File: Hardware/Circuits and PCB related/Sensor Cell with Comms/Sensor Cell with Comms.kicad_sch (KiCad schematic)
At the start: 57 parts, among them J1 Conn_01x02_Shielded, U1 TCAN337, U10 FM24V05, U2 MCP2518FD-xQBB, U3 STM32F103C6Tx, U4 TPS22950x, U5 TPS2421, U6 TPS2421, U7 TMP75B, U8 TMP75B, U9 TMP75B, Y1 DSC6111B

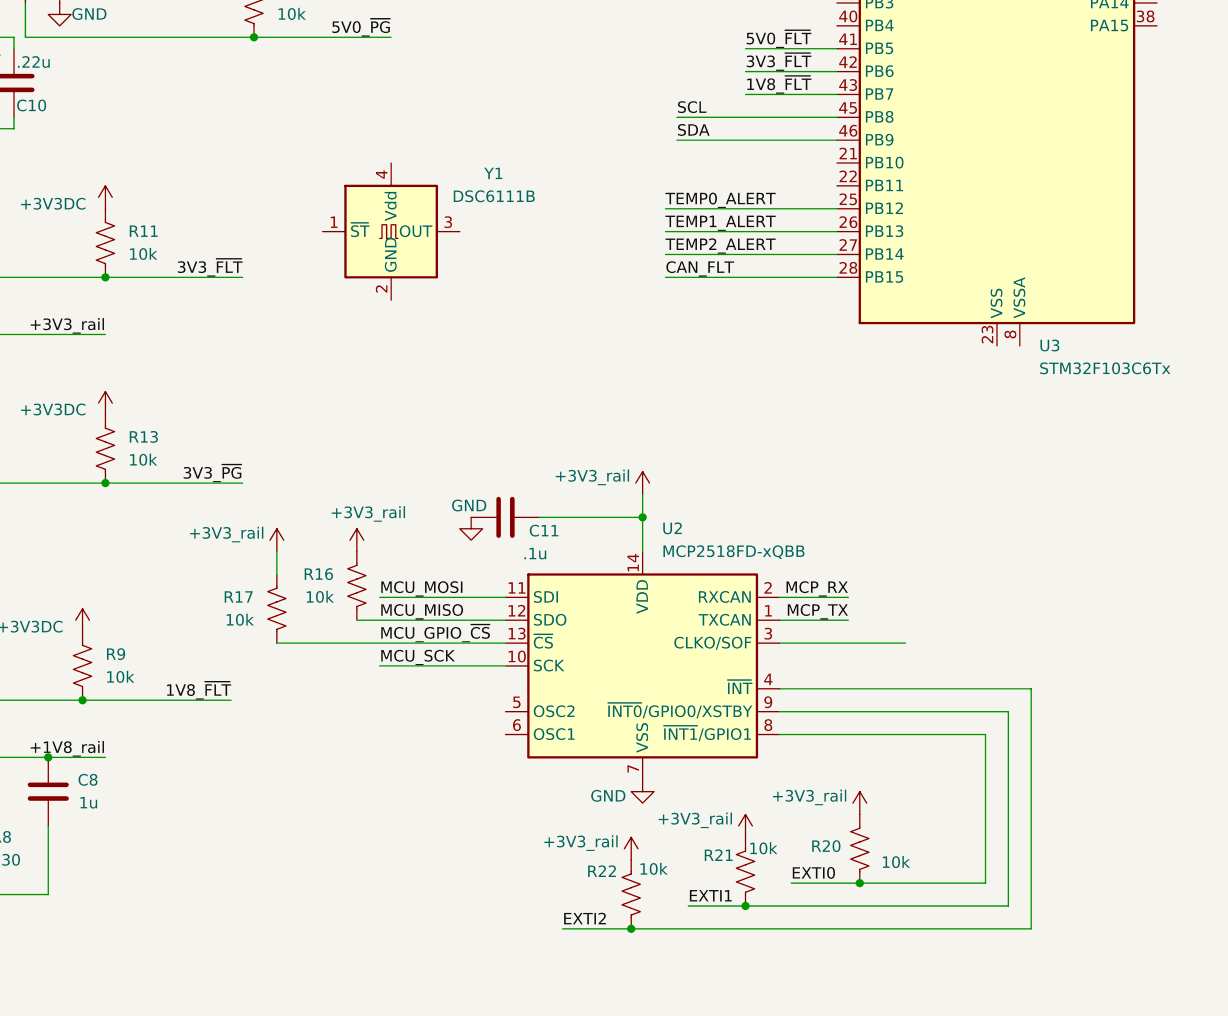
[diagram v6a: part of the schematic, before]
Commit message: Footprint for Osc done, osc wired to MCP and STM wired to Osc. I need to make the pcb now, and then determine what type of connector to use. Things to keep in mind when choosing; Needs to either support power and data, or we can separate out the data and power bus to different connectors. Look into after the interface doc is finalized or closer to completion. Start integration to connect the two small subsystems together for demo
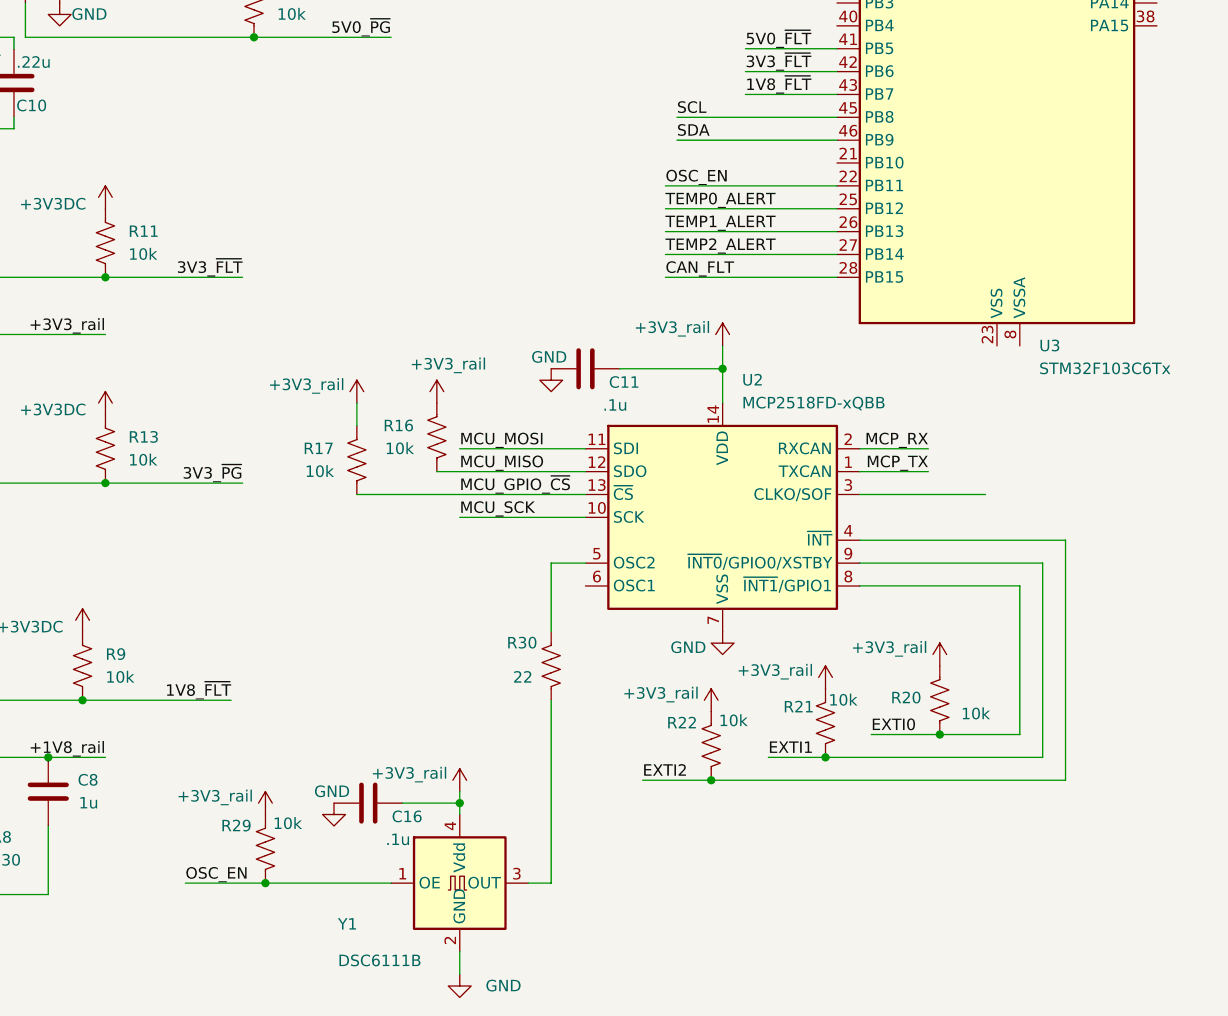
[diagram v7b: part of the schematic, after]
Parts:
- added C16: .1u, Capacitor_SMD:C_0603_1608Metric_Pad1.08x0.95mm_HandSolder, symbol Device:C
- added R29: 10k, Resistor_SMD:R_0603_1608Metric_Pad0.98x0.95mm_HandSolder, symbol Device:R_US
- added R30: 22, Resistor_SMD:R_0603_1608Metric_Pad0.98x0.95mm_HandSolder, symbol Device:R_US
- Y1: footprint footprintLib:VDFN-4_5x3.2mm_P2.54BSC -> Oscillator:Oscillator_SMD_SiT_PQFN-4Pin_2.0x1.6mm
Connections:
- net +3V3_rail: now also Y1.4 (Vdd), C16.2, R29.2
- net GND: now also Y1.2 (GND), C16.1
- net OSC_EN: now reaches Y1.1 (OE)
- net OSC_EN: now also U3.22 (PB11), R29.1
- net at Y1.3 (OUT): now also R30.1
- net at U2.5 (OSC2): now also R30.2
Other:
- moved on the sheet: C11, R16, R17, R20, R21, R22, U2, Y1

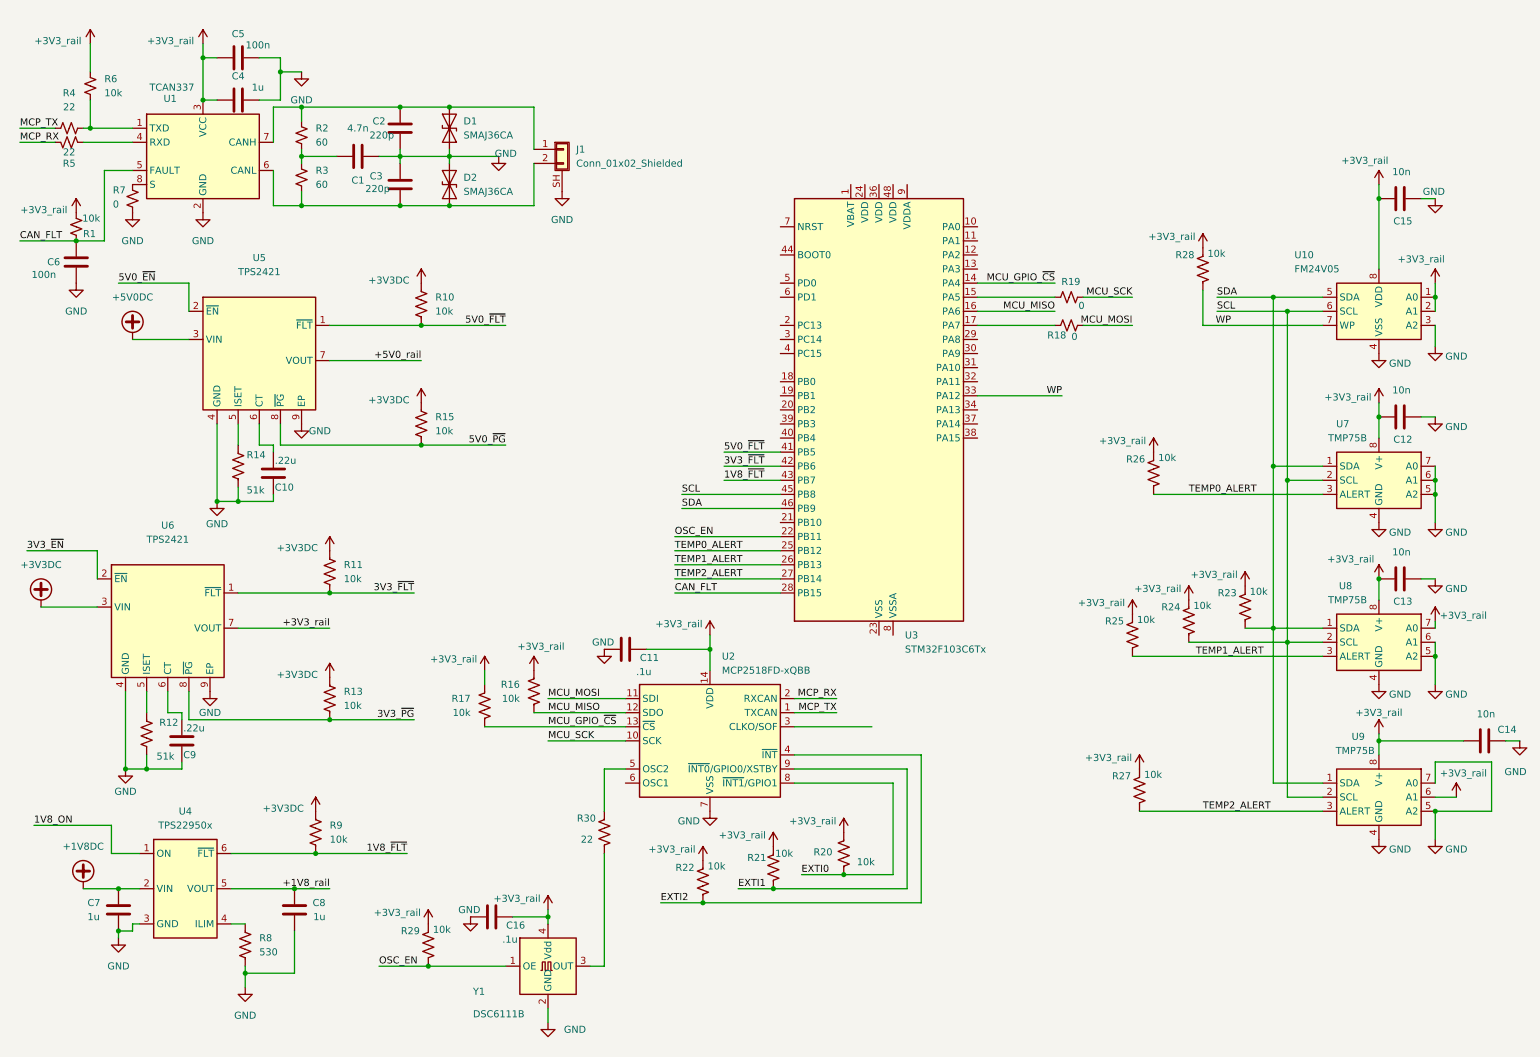
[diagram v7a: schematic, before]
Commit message: Added breakout header pins to footprints for STM and MCP2518, need to make MCU master table, EXTI# summary table, and device connection table
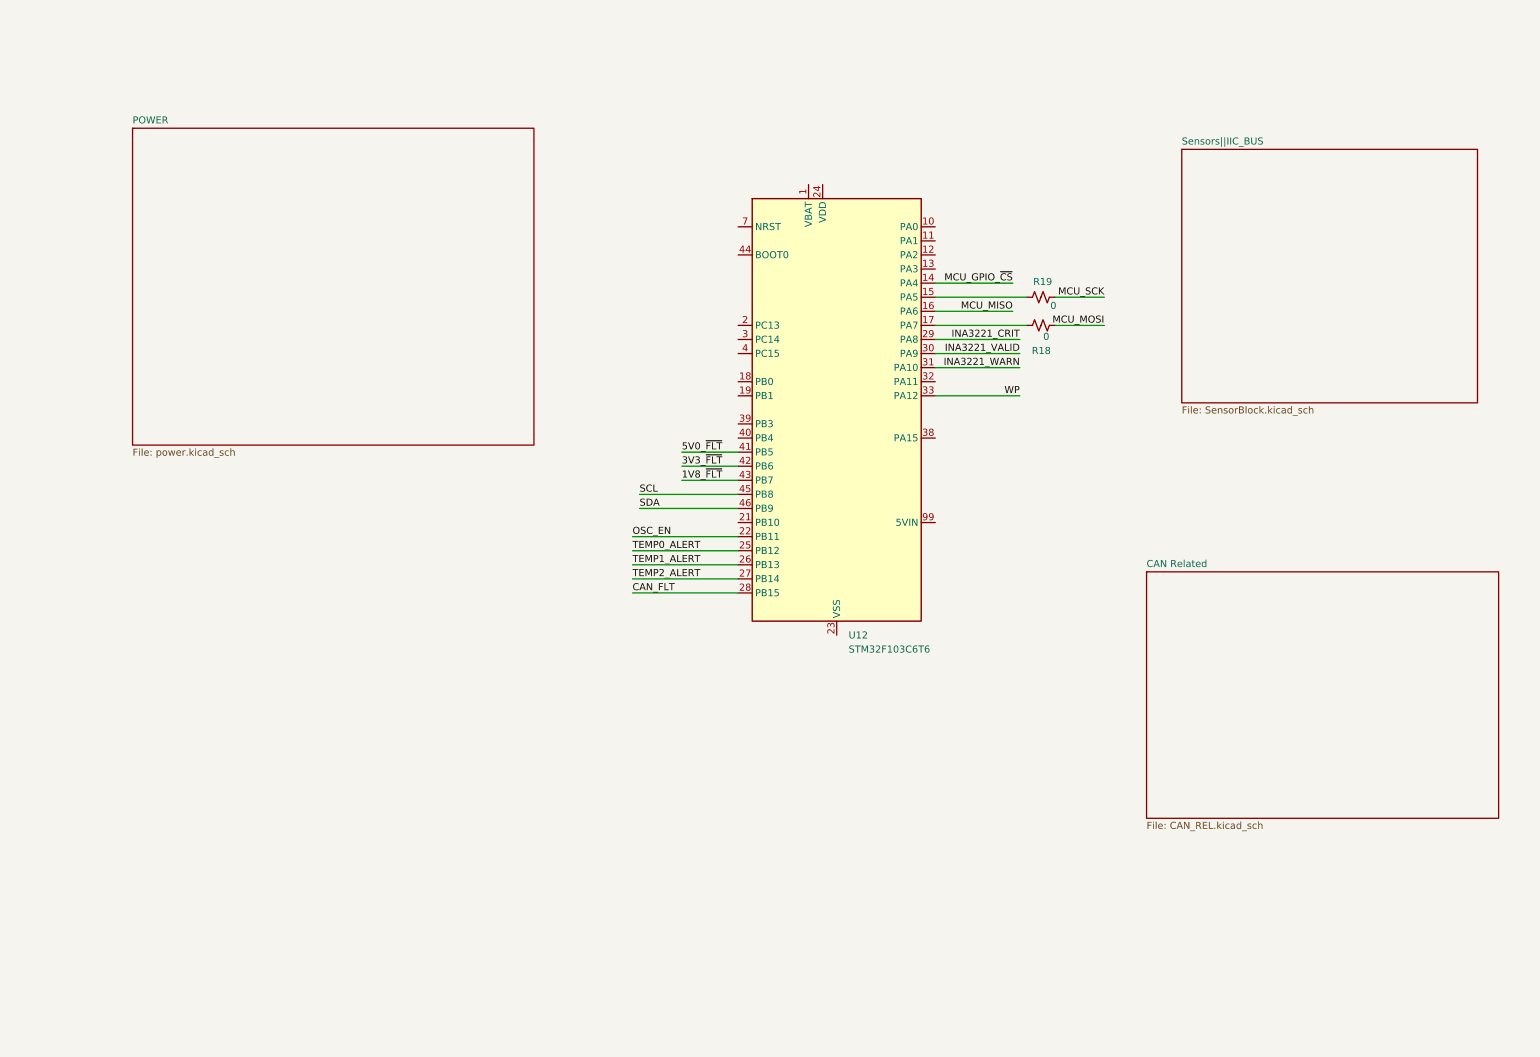
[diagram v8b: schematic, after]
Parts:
- removed C1: 4.7n, Capacitor_SMD:C_0603_1608Metric_Pad1.08x0.95mm_HandSolder, symbol Device:C
- removed C10, C9: .22u, Capacitor_SMD:C_0603_1608Metric_Pad1.08x0.95mm_HandSolder, symbol Device:C
- removed C11, C16: .1u, Capacitor_SMD:C_0603_1608Metric_Pad1.08x0.95mm_HandSolder, symbol Device:C
- removed C12, C13, C14, C15: 10n, Capacitor_SMD:C_0201_0603Metric_Pad0.64x0.40mm_HandSolder, symbol Device:C
- removed C2, C3: 220p, Capacitor_SMD:C_0603_1608Metric_Pad1.08x0.95mm_HandSolder, symbol Device:C
- removed C4, C7, C8: 1u, Capacitor_SMD:C_0603_1608Metric_Pad1.08x0.95mm_HandSolder, symbol Device:C
- removed C5, C6: 100n, Capacitor_SMD:C_0603_1608Metric_Pad1.08x0.95mm_HandSolder, symbol Device:C
- removed D1, D2: SMAJ36CA, Diode_SMD:D_SMA, symbol Diode:SMAJ36CA
- removed J1: Conn_01x02_Shielded, symbol Connector_Generic_Shielded:Conn_01x02_Shielded
- removed R1, R6: 10k, Resistor_SMD:R_0603_1608Metric_Pad0.98x0.95mm_HandSolder, symbol Device:R_Small_US
- removed R10, R11, R13, R15, R16, R17, R20, R21, R22, R23, R24, R25, R26, R27, R28, R29, R9: 10k, Resistor_SMD:R_0603_1608Metric_Pad0.98x0.95mm_HandSolder, symbol Device:R_US
- removed R12, R14: 51k, Resistor_SMD:R_0603_1608Metric_Pad0.98x0.95mm_HandSolder, symbol Device:R_US
- removed R2, R3: 60, Resistor_SMD:R_0603_1608Metric_Pad0.98x0.95mm_HandSolder, symbol Device:R_Small_US
- removed R30: 22, Resistor_SMD:R_0603_1608Metric_Pad0.98x0.95mm_HandSolder, symbol Device:R_US
- removed R4, R5: 22, Resistor_SMD:R_0603_1608Metric_Pad0.98x0.95mm_HandSolder, symbol Device:R_Small_US
- removed R7: 0, Resistor_SMD:R_0603_1608Metric_Pad0.98x0.95mm_HandSolder, symbol Device:R_Small_US
- removed R8: 530, Resistor_SMD:R_0603_1608Metric_Pad0.98x0.95mm_HandSolder, symbol Device:R_US
- removed U1: TCAN337, Package_SO:SOIC-8_3.9x4.9mm_P1.27mm, symbol Interface_CAN_LIN:TCAN337
- removed U10: FM24V05, Package_SO:SOIC-8_3.9x4.9mm_P1.27mm, symbol Custom Power:FM24V05
- removed U2: MCP2518FD-xQBB, Package_SO:SOIC-14_3.9x8.7mm_P1.27mm, symbol Interface_CAN_LIN:MCP2518FD-xQBB
- removed U3: STM32F103C6Tx, Package_QFP:LQFP-48_7x7mm_P0.5mm, symbol MCU_ST_STM32F1:STM32F103C6Tx
- removed U4: TPS22950x, Package_TO_SOT_SMD:SOT-23-6, symbol Custom Power:TPS22950x
- removed U5, U6: TPS2421, Package_SO:HSOP-8-1EP_3.9x4.9mm_P1.27mm_EP2.41x3.1mm_ThermalVias, symbol Custom Power:TPS2421
- removed U7, U8, U9: TMP75B, Package_SO:SO-8_3.9x4.9mm_P1.27mm, symbol Sensor_Temperature:TMP1075D
- removed Y1: DSC6111B, Oscillator:Oscillator_SMD_SiT_PQFN-4Pin_2.0x1.6mm, symbol Custom Power:DSC61XXB
- added U12: STM32F103C6T6, footprintLib:PinHeader_1x20_P1.00mm_Verticalx2, symbol Custom Power:custom
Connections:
- net 1V8_~{FLT}: now also U12.43 (PB7)
- net 3V3_~{FLT}: now also U12.42 (PB6)
- net 5V0_~{FLT}: now also U12.41 (PB5)
- net CAN_FLT: now also U12.28 (PB15)
- net MCU_GPIO_~{CS}: now also U12.14 (PA4)
- net MCU_MISO: now also U12.16 (PA6)
- net OSC_EN: now also U12.22 (PB11)
- net SCL: now also U12.45 (PB8)
- net SDA: now also U12.46 (PB9)
- net TEMP0_ALERT: now also U12.25 (PB12)
- net TEMP1_ALERT: now also U12.26 (PB13)
- net TEMP2_ALERT: now also U12.27 (PB14)
- net WP: now also U12.33 (PA12)
- net at R18.2: now also U12.17 (PA7)
- net at R19.2: now also U12.15 (PA5)
- new net: U12.23 (VSS), U12.35 (VSS), U12.47 (VSS)
- new net INA3221_CRIT: U12.29 (PA8)
- new net INA3221_VALID: U12.30 (PA9)
- new net INA3221_WARN: U12.31 (PA10)
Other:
- added sheet CAN Related (CAN_REL.kicad_sch)
- added sheet POWER (power.kicad_sch)
- added sheet Sensors||IIC_BUS (SensorBlock.kicad_sch)
- moved on the sheet: R18, R19
